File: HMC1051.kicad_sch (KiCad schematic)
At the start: 40 parts

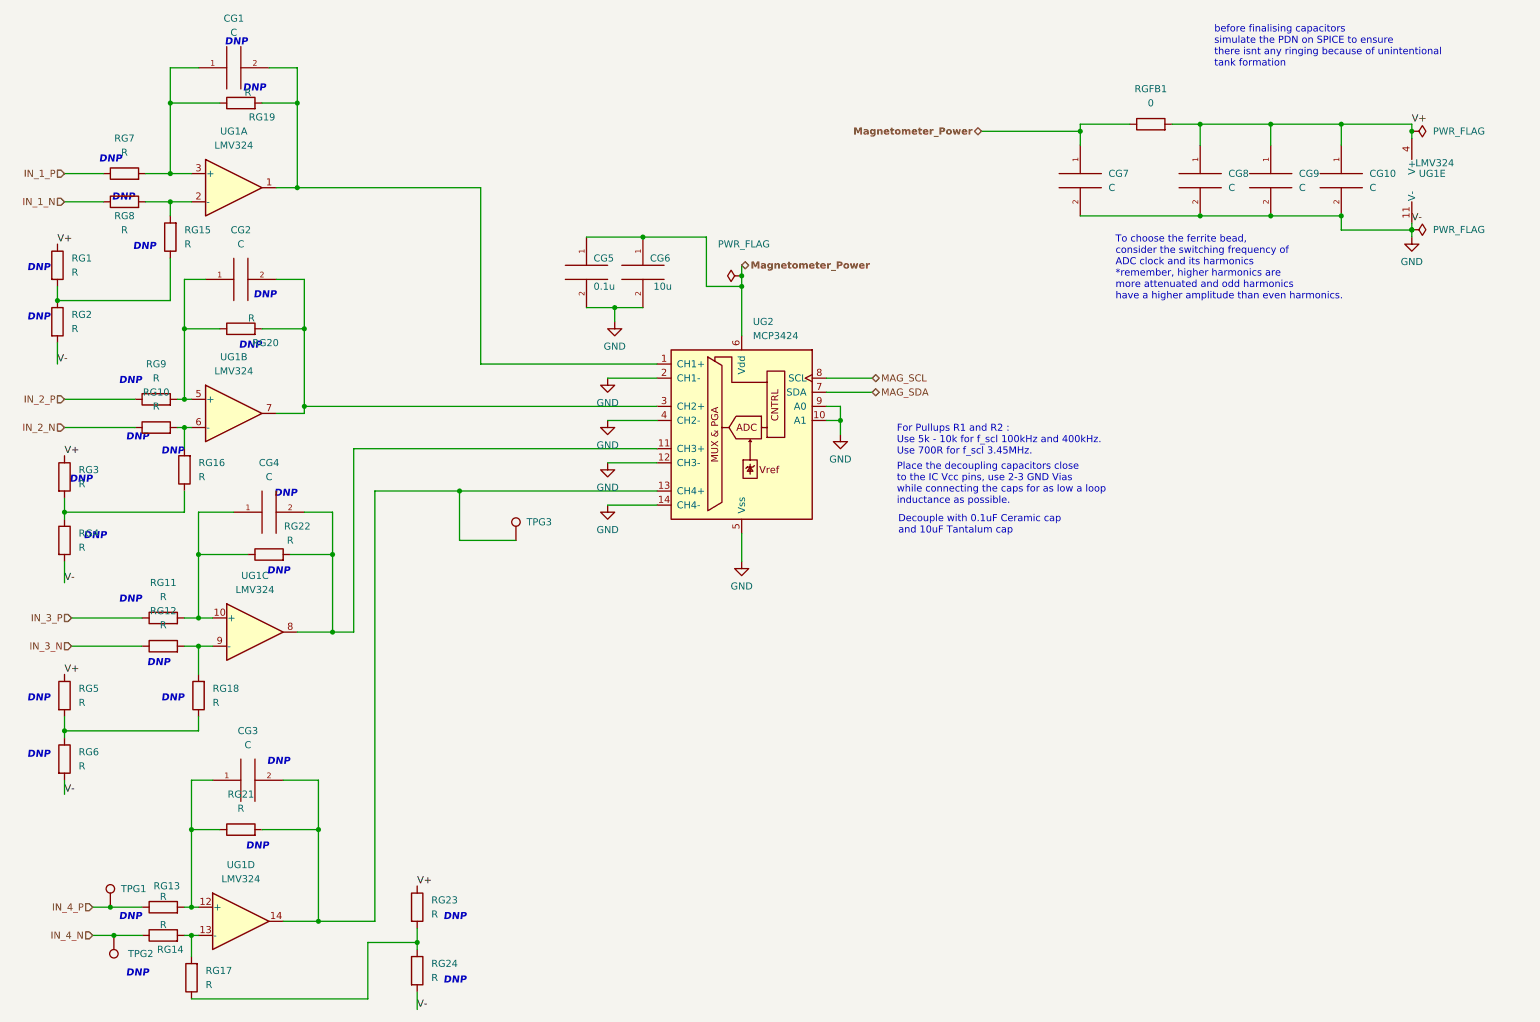
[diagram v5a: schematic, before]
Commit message: MCU circuitry forgot LOL
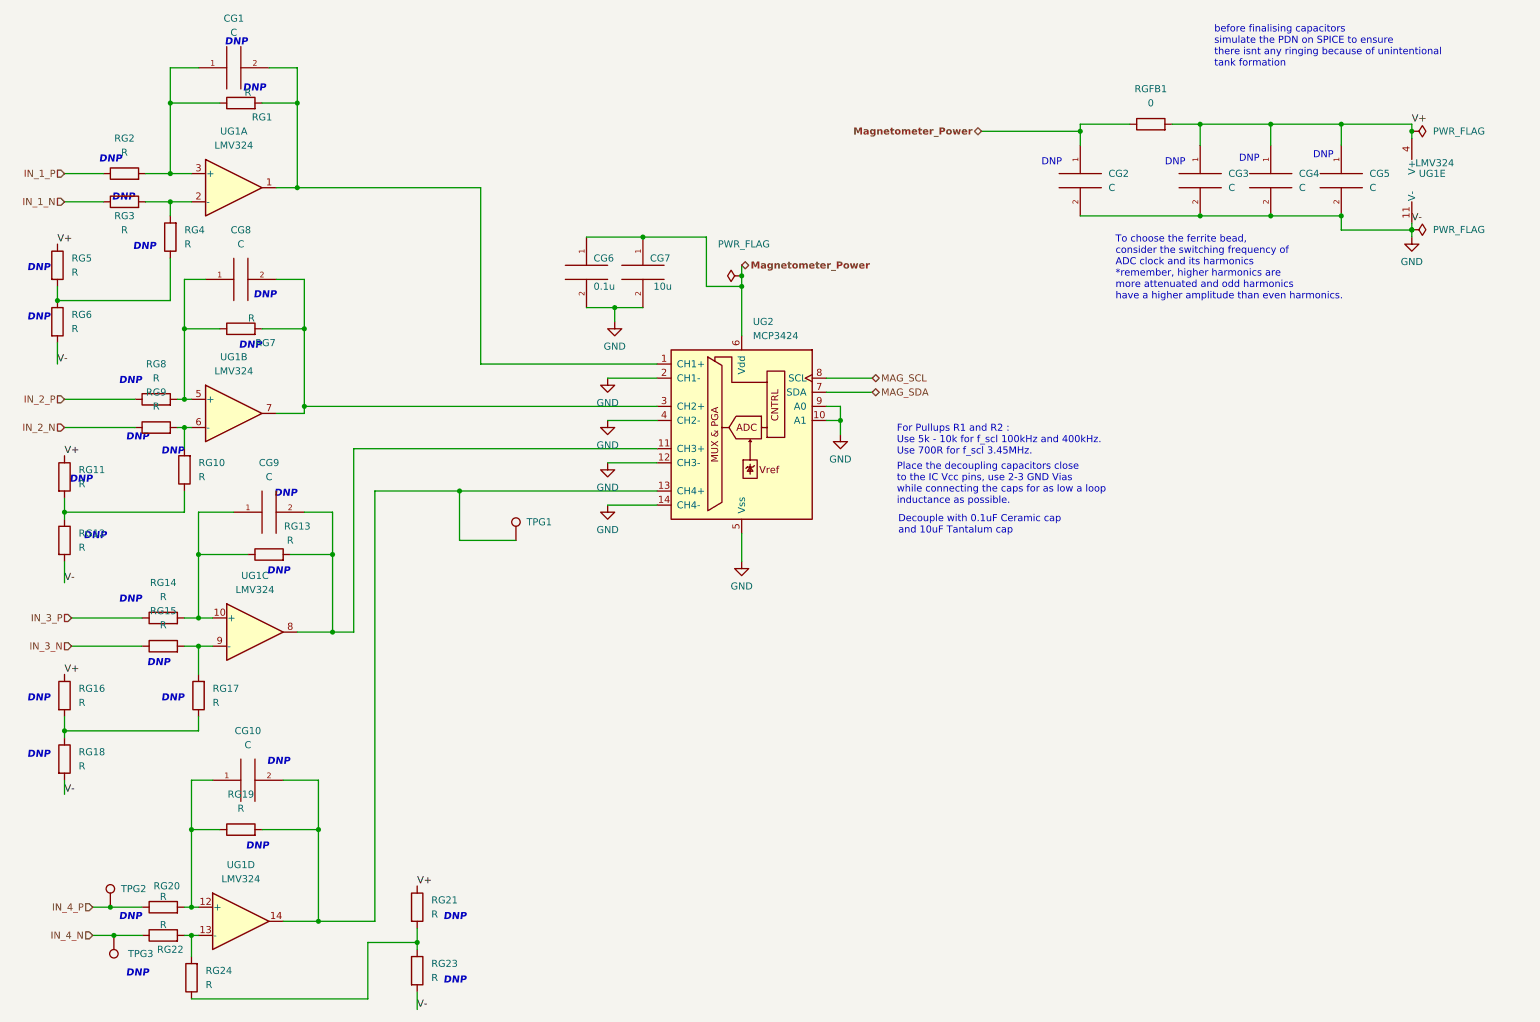
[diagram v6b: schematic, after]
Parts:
- renumbered CG3 to CG10, CG7 to CG2, CG8 to CG3, CG9 to CG4, CG10 to CG5, CG5 to CG6, CG6 to CG7, CG2 to CG8, CG4 to CG9, RG19 to RG1, RG16 to RG10, RG3 to RG11, RG4 to RG12, RG22 to RG13, RG11 to RG14, RG12 to RG15, RG5 to RG16, RG18 to RG17, RG6 to RG18, RG21 to RG19, RG7 to RG2, RG13 to RG20, RG23 to RG21, RG14 to RG22, RG24 to RG23, RG17 to RG24, RG8 to RG3, RG15 to RG4, RG1 to RG5, RG2 to RG6, RG20 to RG7, RG9 to RG8, RG10 to RG9, TPG3 to TPG1, TPG1 to TPG2, TPG2 to TPG3

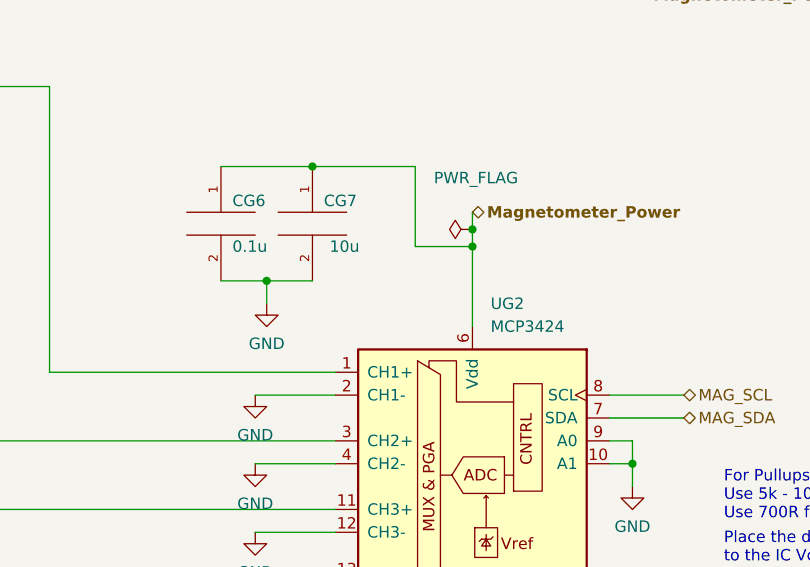
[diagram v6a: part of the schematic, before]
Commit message: ADC tantalum cap PN added
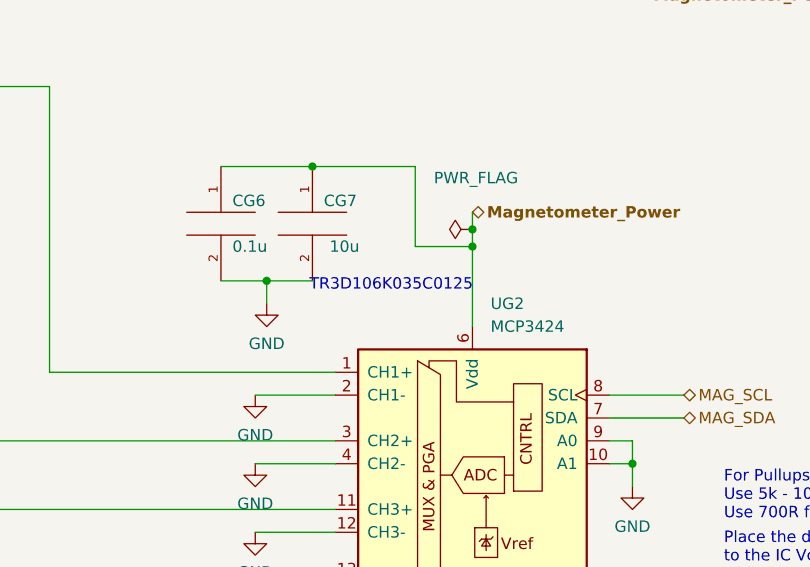
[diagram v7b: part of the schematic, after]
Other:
- note added: "TR3D106K035C0125"
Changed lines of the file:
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@@
     (effects (font (size 1.27 1.27) bold italic) (justify right bottom))
+  )
+  (text "\n    TR3D106K035C0125" (at 127 71.12 0)
+    (effects (font (size 1.27 1.27)) (justify left bottom))
   )
   (text "DNP" (at 35.7804 43.9447 180)
